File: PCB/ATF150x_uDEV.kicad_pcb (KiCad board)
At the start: 2 copper layers, 50.8 x 20.3 mm, 14 parts, among them J1 Altera JTAG-A+VPP, J2 1x20x2.54mm, J3 1x20x2.54mm, U1 ATF150x-xAx44

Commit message: fillet tracks
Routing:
- net VCCIO: track 64.4 -> 65.9 mm
- net /26/TCK: track 46.8 -> 45.9 mm
- net VCCINT: track 51.8 -> 51.2 mm

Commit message: fillet tracks, silkscreen, 3d models
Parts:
- moved C1 0.12 mm to (142.1, 105.3)
- moved C3 0.11 mm to (149.2, 103.6)
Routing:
- net VCCIO: track 65.9 -> 64.2 mm
- net GND: vias 37 -> 53

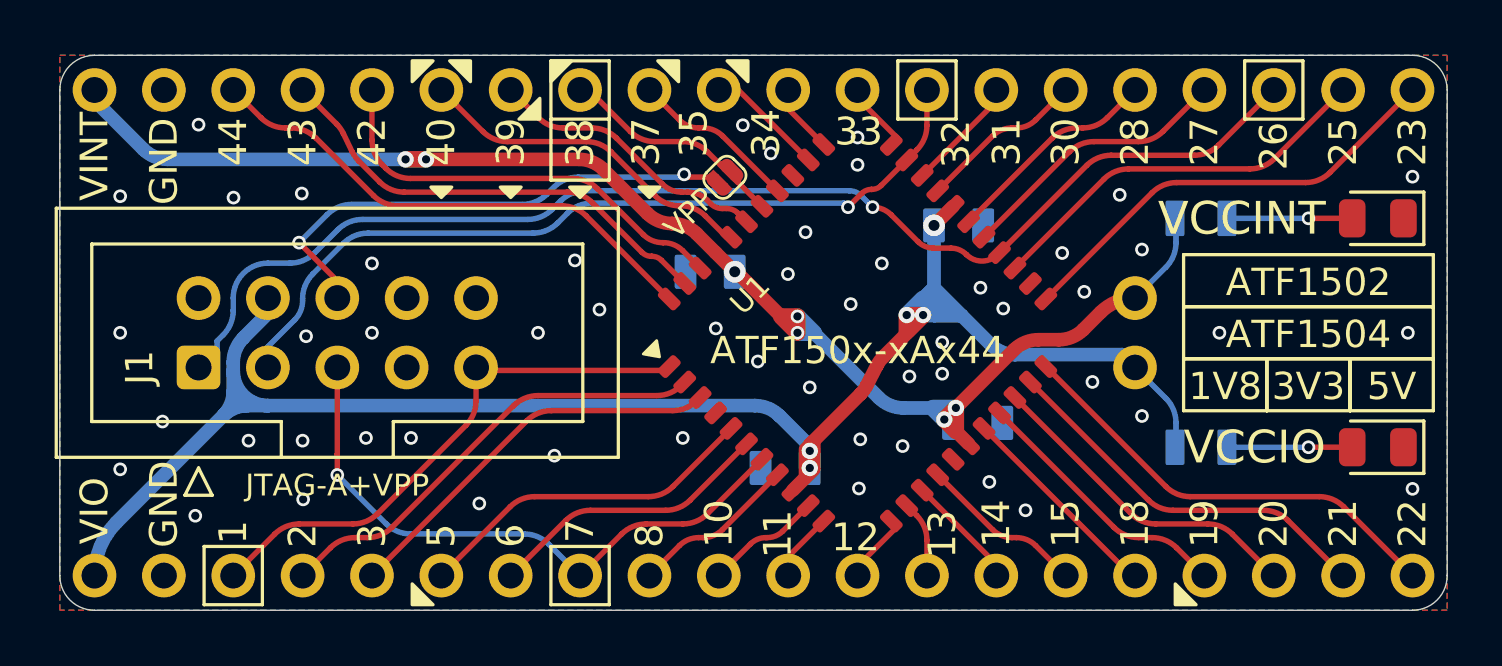
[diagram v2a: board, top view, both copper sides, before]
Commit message: streamline traces, eliminate a via
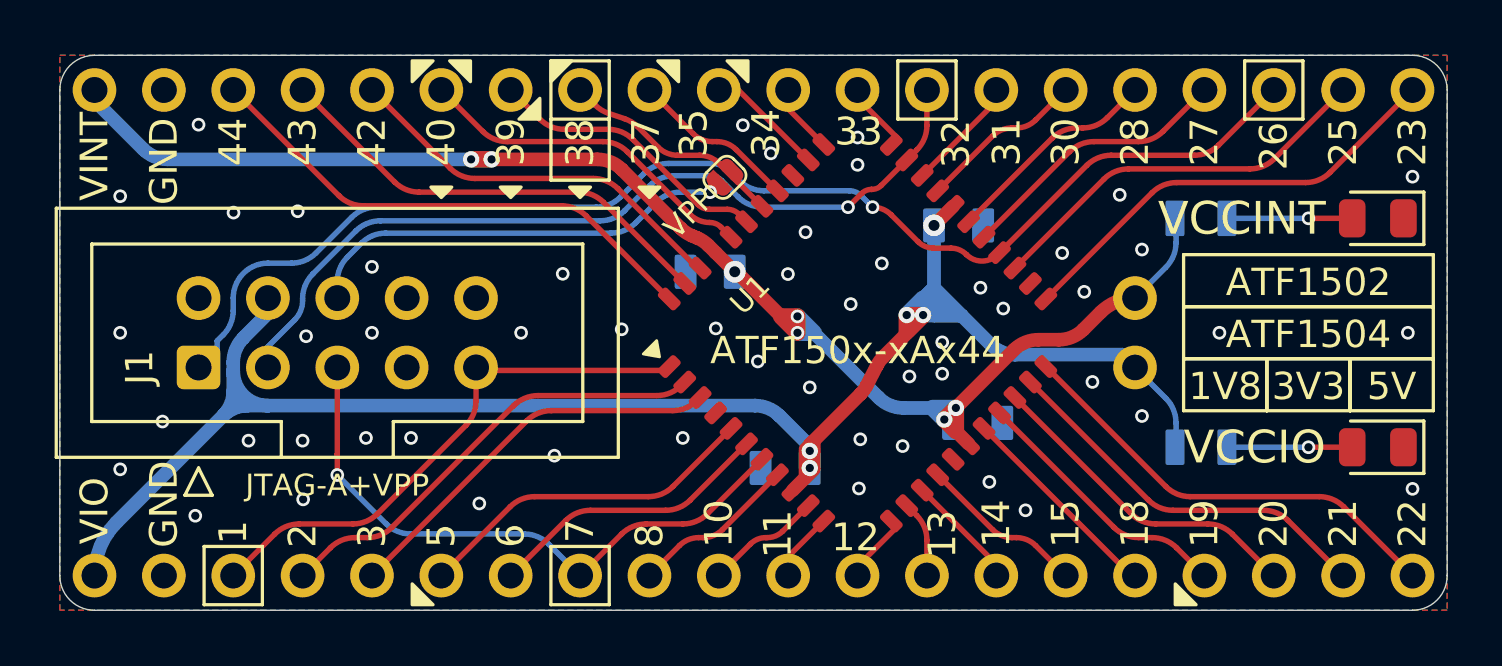
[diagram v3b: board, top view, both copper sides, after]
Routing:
- net Net-(J1-VPP): track 19.0 -> 16.1 mm, vias 2 -> 1
- net /42: track 15.8 -> 14.6 mm
- net /32/TDO: track 30.2 -> 30.9 mm
- net /26/TCK: track 45.9 -> 46.6 mm
